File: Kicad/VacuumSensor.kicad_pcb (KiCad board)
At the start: 2 copper layers, 56.9 x 47.2 mm, 38 parts, among them IC1 LM2597MX-ADJ_NOPB, IC2 24PCDFA6D, IC3 INA849DR, IC4 TL071CP, IC5 TL071CP, J1 Screw_Terminal_01x03, J2 Conn_01x02, U1 TL431LP, U2 TL431LP

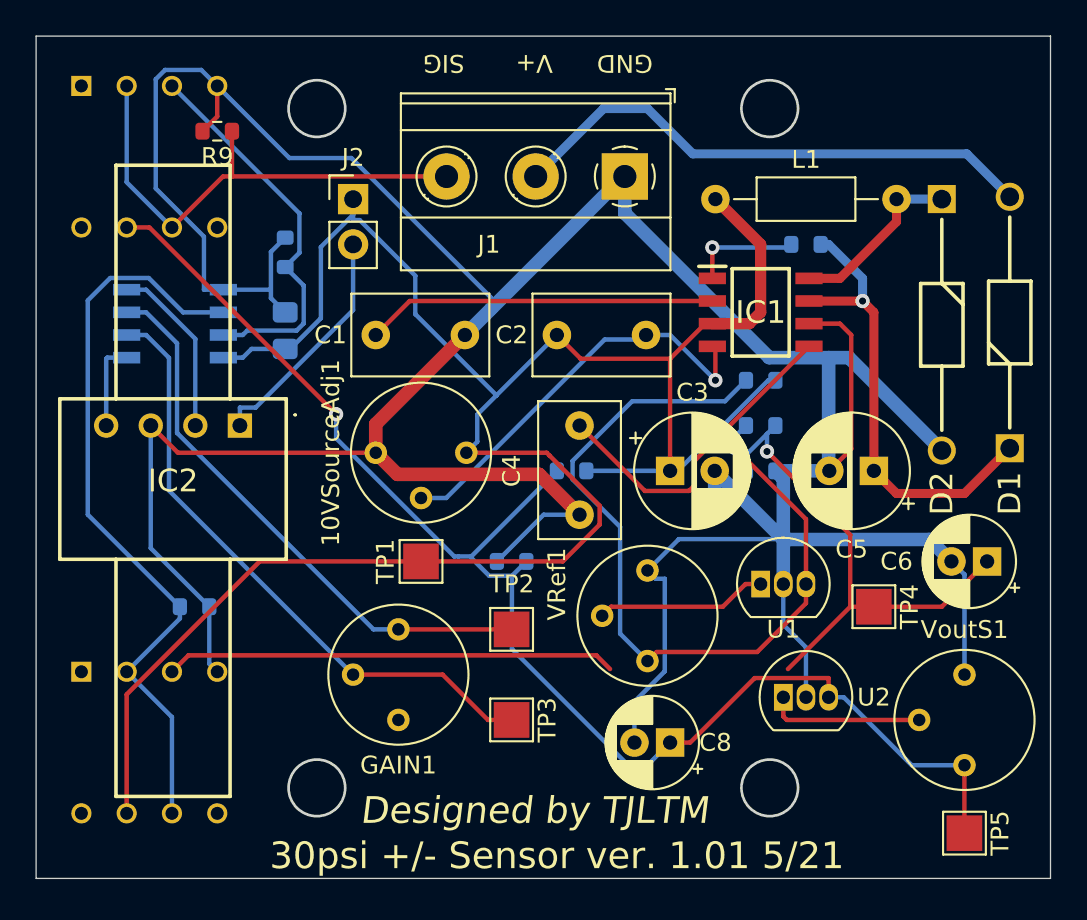
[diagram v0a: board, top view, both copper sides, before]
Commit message: 1.02 update removed the unity gain output op amp and Gain trim pot and replaced it witha  0.1% 665 ohm resistor for the instrumentation amp. simplified the voltage reference and 5v circuits. Added an output Pot to be able to to limit it to 3.3v volts. Added an optional arduino nano v3 and rs232 output. along with a NTC 10k Thermistor for temp compensation calcs.
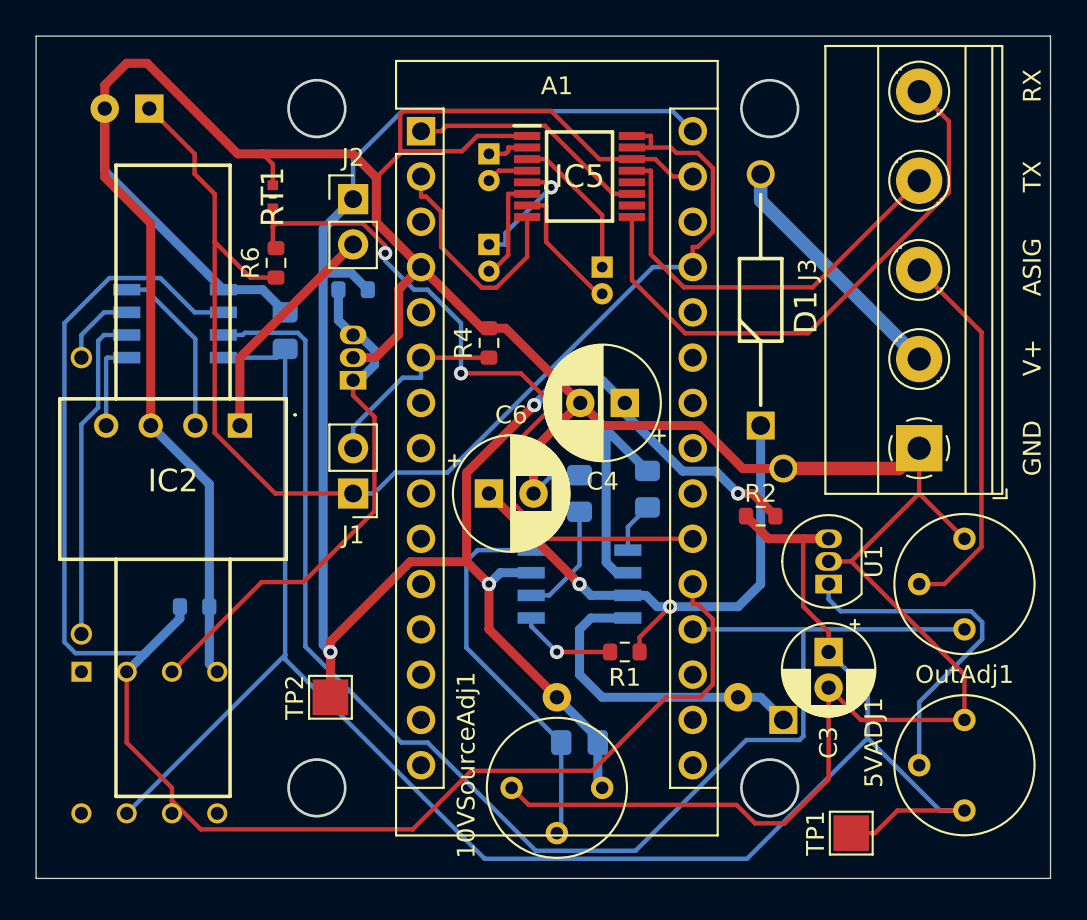
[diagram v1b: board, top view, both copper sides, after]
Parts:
- removed the R3 at (116.8, 101.6)
- removed the R5 at (90.2, 91.9)
- removed R7: 10k, Resistor_SMD:R_0603_1608Metric
- removed R9: 10M, Resistor_SMD:R_0603_1608Metric
- removed the TP2 at (102.9, 113.0)
- removed TP3, TP4, TP5: TestPoint, TestPoint:TestPoint_Pad_2.0x2.0mm
- removed VoutS1: 20k, Potentiometer_THT:Potentiometer_Bourns_3339P_Vertical
- added A1: Arduino_Nano_v3.x, Module:Arduino_Nano, F.Cu at (97.8, 85.1)
- added C10: 0.22uF, Capacitor_THT:CP_Radial_D4.0mm_P1.50mm, B.Cu at (101.6, 91.4)
- added C11: 0.1uF, Capacitor_THT:CP_Radial_D6.3mm_P2.50mm, B.Cu at (82.5, 83.8)
- added C9: 0.22uF, Capacitor_THT:CP_Radial_D4.0mm_P1.50mm, B.Cu at (101.6, 86.4)
- added J3: Screw_Terminal_01x05, TerminalBlock_Phoenix:TerminalBlock_Phoenix_MKDS-1,5-5_1x05_P5.00mm_Horizontal, F.Cu at (125.7, 102.9)
- added R6: 10k, Resistor_SMD:R_0603_1608Metric, F.Cu at (89.7, 92.5)
- added RG1: YR1B665RCC, SamacSys_Parts:RESAD1550W60L630D230, B.Cu at (78.7, 97.8)
- added RT1: NTCSP103JF103FT1S, SamacSys_Parts:THRMC1005X55N, F.Cu at (89.5, 88.8)
- added TP1: TestPoint, TestPoint:TestPoint_Pad_2.0x2.0mm, F.Cu at (121.9, 124.5)
- C1, C2: footprint Capacitor_THT:C_Disc_D7.5mm_W4.4mm_P5.00mm -> Capacitor_SMD:C_0805_2012Metric_Pad1.15x1.40mm_HandSolder; moved to B.Cu
- C5: renamed from C4; footprint Capacitor_THT:C_Disc_D7.5mm_W4.4mm_P5.00mm -> Capacitor_SMD:C_0805_2012Metric_Pad1.15x1.40mm_HandSolder; moved to B.Cu
- C8: value 1uF -> 0.22uF; footprint Capacitor_THT:CP_Radial_D5.0mm_P2.00mm -> Capacitor_THT:CP_Radial_D4.0mm_P1.50mm; moved to B.Cu
- D2, IC1, L1, U2: moved to B.Cu
- IC5: value TL071CP -> SP3220EBEY-L_TR; footprint SamacSys_Parts:DIP794W53P254L959H508Q8N -> SamacSys_Parts:SOP65P640X120-16N; moved to F.Cu
- J1: value Screw_Terminal_01x03 -> Conn_01x02; footprint TerminalBlock_Phoenix:TerminalBlock_Phoenix_MKDS-1,5-3_1x03_P5.00mm_Horizontal -> Connector_PinHeader_2.54mm:PinHeader_1x02_P2.54mm_Vertical
- OutAdj1: renamed from GAIN1; value 5k -> 1M
- R1, R2: moved to F.Cu
- R4: value 10k -> 20k; moved to F.Cu
- moved OutAdj1 32.2 mm to (128.3, 113.0)
- moved D2 30.5 mm to (118.1, 118.1), turned to 90 degrees
- moved U2 30.0 mm to (94.0, 99.1), turned to 90 degrees
- moved L1 29.3 mm to (105.4, 116.8)
- moved C8 26.9 mm to (108.0, 92.7), turned to 270 degrees
- moved R1 25.0 mm to (109.2, 114.3)
- moved IC5 24.2 mm to (106.7, 87.6), turned to 0 degrees
- moved J1 23.4 mm to (94.0, 105.4)
- moved C2 22.9 mm to (106.7, 119.4), turned to 180 degrees
- moved C6 21.6 mm to (101.6, 105.4), turned to 0 degrees
- moved 10VSourceAdj1 20.3 mm to (108.0, 121.9)
- moved 5VADJ1 19.7 mm to (128.3, 123.2)
- moved IC1 18.3 mm to (106.7, 110.5)
- moved R4 16.8 mm to (101.6, 97.0), turned to 90 degrees
- moved R3 15.9 mm to (94.0, 94.0)
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- renumbered VRef1 to 5VADJ1, C6 to C3, C3 to C4, C5 to C6, R6 to R3, R8 to R5, TP1 to TP2
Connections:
- 5VADJ1 pad 1: Net-(R2-Pad2) -> +5V
- C3 pad 1: Net-(C6-Pad1) -> +5V
- C7 pad 1: +10V -> +5V
- C8 pad 2: GND -> Net-(C8-Pad2)
- IC3 pad 2: Net-(GAIN1-Pad2) -> Net-(IC3-Pad2)
- IC3 pad 3: Net-(GAIN1-Pad3) -> Net-(IC3-Pad3)
- IC3 pad 7: Net-(IC3-Pad7) -> Net-(A1-Pad19)
- IC3 pad 8: +10V -> +5V
- IC4 pad 3: Net-(C6-Pad1) -> Net-(IC4-Pad3)
- IC4 pad 7: +10V -> +5V
- IC5 pad 1: (no net) -> GND
- IC5 pad 2: Net-(IC5-Pad2) -> Net-(C9-Pad1)
- IC5 pad 3: Net-(IC3-Pad7) -> Net-(C8-Pad1)
- IC5 pad 4: GND -> Net-(C9-Pad2)
- IC5 pad 5: (no net) -> Net-(C10-Pad1)
- IC5 pad 6: Net-(IC5-Pad2) -> Net-(C10-Pad2)
- IC5 pad 7: Net-(C8-Pad1) -> Net-(C8-Pad2)
- IC5 pad 8: (no net) -> Net-(A1-Pad2)
- J1 pad 1: GND -> Net-(A1-Pad27)
- J1 pad 2: Net-(D1-Pad2) -> Net-(A1-Pad6)
- OutAdj1 pad 1: (no net) -> Net-(A1-Pad19)
- OutAdj1 pad 2: Net-(GAIN1-Pad2) -> Net-(J3-Pad3)
- OutAdj1 pad 3: Net-(GAIN1-Pad3) -> GND
- R2 pad 2: Net-(R2-Pad2) -> +5V
- R3 pad 2: Net-(C8-Pad1) -> Net-(IC4-Pad3)
- R4 pad 1: Net-(C6-Pad1) -> Net-(A1-Pad6)
- U1 pad 3: Net-(R2-Pad2) -> +5V
- U2 pad 1: Net-(U2-Pad1) -> Net-(IC4-Pad3)
- U2 pad 3: Net-(C8-Pad1) -> Net-(IC4-Pad3)
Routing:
- net +5V: track 0.00 -> 105.6 mm
- net Net-(A1-Pad19): track 0.00 -> 78.6 mm
- net Net-(C8-Pad1): track 79.0 -> 8.42 mm, vias 1 -> 0
- net Net-(A1-Pad27): track 0.00 -> 70.4 mm
- net Net-(C6-Pad1): track 53.8 -> 0.00 mm, vias 1 -> 0
- net Net-(R2-Pad2): track 46.7 -> 0.00 mm, vias 1 -> 0
- net Net-(A1-Pad20): track 42.1 -> 87.9 mm
- net Net-(A1-Pad21): track 0.00 -> 41.5 mm, vias 0 -> 2
- net Net-(GAIN1-Pad2): track 34.9 -> 0.00 mm
- net Net-(IC5-Pad9): track 0.00 -> 32.2 mm
- net Net-(GAIN1-Pad3): track 31.9 -> 0.00 mm
- net Net-(IC4-Pad3): track 0.00 -> 29.7 mm
- net Net-(IC5-Pad2): track 28.1 -> 0.00 mm
- net Net-(IC5-Pad13): track 0.00 -> 24.0 mm
- net Net-(IC3-Pad7): track 21.8 -> 0.00 mm
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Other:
- board text added: "30psi +/- Sensor ver. 1.02 6/21"
- board text added: "ASIG"
- board text added: "RX"
- board text added: "TX"
- board text removed: "30psi +/- Sensor ver. 1.01 5/21"
- board text removed: "SIG"
